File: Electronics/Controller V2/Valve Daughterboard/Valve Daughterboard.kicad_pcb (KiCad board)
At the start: 2 copper layers, 68.5 x 87.5 mm, 30 parts, among them J1 Conn_01x08, J10 Conn_01x10, J11 Conn_01x02, J12 Conn_01x02, J13 Conn_01x02, J14 Conn_01x02, J15 Conn_01x02, J16 Conn_01x02, J17 Conn_01x02, J18 Conn_01x02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

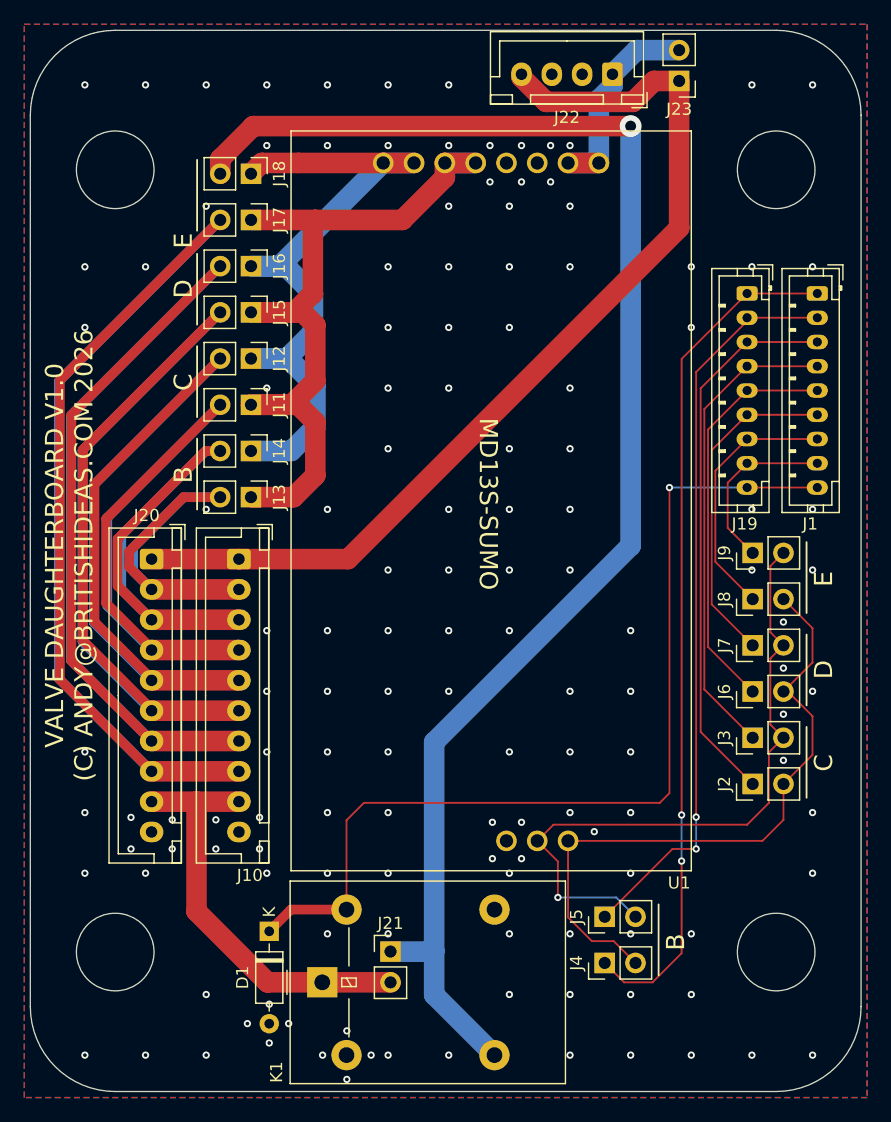
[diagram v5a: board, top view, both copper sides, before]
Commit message: Added jumper to bypass current sensing. Minor tweaks. Generated production files.
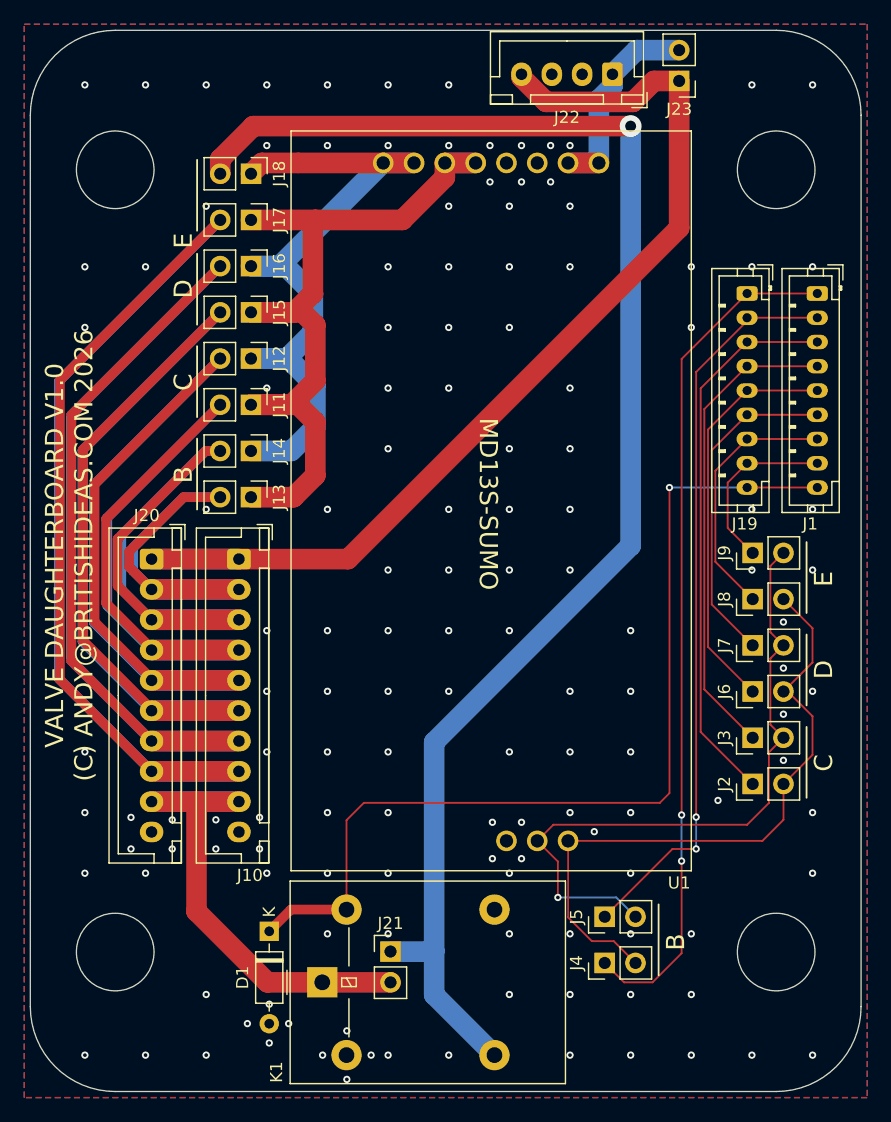
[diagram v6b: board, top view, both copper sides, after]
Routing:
- net /VALVE_C_MA: track 58.5 -> 65.7 mm
- net /VALVE_E_MB: track 34.7 -> 41.9 mm
- net /VALVE_D_MA: track 87.0 -> 94.2 mm
- net /VALVE_B_MB: track 45.5 -> 52.7 mm
- net /VALVE_B_MA: track 33.4 -> 40.6 mm
- net +12V: track 81.7 -> 88.9 mm
- net /VALVE_E_MA: track 115.4 -> 122.6 mm
- net /VALVE_D_MB: track 101.2 -> 108.4 mm
- net /VALVE_C_MB: track 72.8 -> 80.0 mm
- net GND: vias 138 -> 139
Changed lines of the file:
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@@
     (fp_line (start 24.95 3.4) (end 24.95 -2.35)
       (stroke (width 0.1) (type solid)) (layer "F.Fab"))
-    (pad "1" thru_hole roundrect (at 0 0 270) (size 1.7 1.95) (drill 0.95) (layers "*.Cu" "*.Mask") (roundrect_rratio 0.147059)
+    (pad "1" thru_hole roundrect (at 0 0 270) (size 1.7 1.95) (drill 0.95) (layers "*.Cu" "*.Mask") (roundrect_rratio 0.1470588235)
       (net 11 "+12V") (pinfunction "Pin_1") (pintype "passive"))
     (pad "2" thru_hole oval (at 2.5 0 270) (size 1.7 1.95) (drill 0.95) (layers "*.Cu" "*.Mask")
@@
     (fp_line (start 9.95 3.4) (end 9.95 -2.35)
       (stroke (width 0.1) (type solid)) (layer "F.Fab"))
-    (pad "1" thru_hole roundrect (at 0 0 180) (size 1.7 1.95) (drill 0.95) (layers "*.Cu" "*.Mask") (roundrect_rratio 0.147059)
+    (pad "1" thru_hole roundrect (at 0 0 180) (size 1.7 1.95) (drill 0.95) (layers "*.Cu" "*.Mask") (roundrect_rratio 0.1470588235)
       (net 26 "VDD") (pinfunction "Pin_1") (pintype "passive"))
     (pad "2" thru_hole oval (at 2.5 0 180) (size 1.7 1.95) (drill 0.95) (layers "*.Cu" "*.Mask")
@@
     (fp_line (start 17.95 2.8) (end 17.95 -1.7)
       (stroke (width 0.1) (type solid)) (layer "F.Fab"))
-    (pad "1" thru_hole roundrect (at 0 0 270) (size 1.2 1.75) (drill 0.75) (layers "*.Cu" "*.Mask") (roundrect_rratio 0.208333)
+    (pad "1" thru_hole roundrect (at 0 0 270) (size 1.2 1.75) (drill 0.75) (layers "*.Cu" "*.Mask") (roundrect_rratio 0.2083333333)
       (net 1 "/VALVE_B_DIR") (pinfunction "Pin_1") (pintype "passive"))
     (pad "2" thru_hole oval (at 2 0 270) (size 1.2 1.75) (drill 0.75) (layers "*.Cu" "*.Mask")
@@
     (fp_line (start 24.95 3.4) (end 24.95 -2.35)
       (stroke (width 0.1) (type solid)) (layer "F.Fab"))
-    (pad "1" thru_hole roundrect (at 0 0 270) (size 1.7 1.95) (drill 0.95) (layers "*.Cu" "*.Mask") (roundrect_rratio 0.147059)
+    (pad "1" thru_hole roundrect (at 0 0 270) (size 1.7 1.95) (drill 0.95) (layers "*.Cu" "*.Mask") (roundrect_rratio 0.1470588235)
       (net 11 "+12V") (pinfunction "Pin_1") (pintype "passive"))
     (pad "2" thru_hole oval (at 2.5 0 270) (size 1.7 1.95) (drill 0.95) (layers "*.Cu" "*.Mask")
@@
     (fp_line (start 17.95 2.8) (end 17.95 -1.7)
       (stroke (width 0.1) (type solid)) (layer "F.Fab"))
-    (pad "1" thru_hole roundrect (at 0 0 270) (size 1.2 1.75) (drill 0.75) (layers "*.Cu" "*.Mask") (roundrect_rratio 0.208333)
+    (pad "1" thru_hole roundrect (at 0 0 270) (size 1.2 1.75) (drill 0.75) (layers "*.Cu" "*.Mask") (roundrect_rratio 0.2083333333)
       (net 1 "/VALVE_B_DIR") (pinfunction "Pin_1") (pintype "passive"))
     (pad "2" thru_hole oval (at 2 0 270) (size 1.2 1.75) (drill 0.75) (layers "*.Cu" "*.Mask")
@@
   (segment (start 132.925 52.675) (end 131.2 54.4) (width 1.7) (layer "F.Cu") (net 11))
   (segment (start 135 64.8) (end 135 52.675) (width 1.7) (layer "F.Cu") (net 11))
+  (segment (start 98.7 92.1) (end 91.5 92.1) (width 1.7) (layer "B.Cu") (net 11))
   (segment (start 89.65 91.483874) (end 89.65 92.75) (width 0.8) (layer "F.Cu") (net 12))
   (segment (start 94.138874 86.995) (end 89.65 91.483874) (width 0.8) (layer "F.Cu") (net 12))
@@
   (segment (start 94.138874 86.995) (end 89.973 91.160874) (width 0.8) (layer "B.Cu") (net 12))
   (segment (start 89.973 93.073) (end 91.5 94.6) (width 0.8) (layer "B.Cu") (net 12))
+  (segment (start 98.7 94.6) (end 91.5 94.6) (width 1.7) (layer "B.Cu") (net 12))
   (segment (start 89.973 91.160874) (end 89.973 93.073) (width 0.8) (layer "B.Cu") (net 12))
   (segment (start 97.155 86.995) (end 94.138874 86.995) (width 0.8) (layer "B.Cu") (net 12))
@@
   (segment (start 95.952919 83.185) (end 89 90.137919) (width 0.8) (layer "B.Cu") (net 13))
   (segment (start 97.155 83.185) (end 95.952919 83.185) (width 0.8) (layer "B.Cu") (net 13))
+  (segment (start 98.7 97.1) (end 91.5 97.1) (width 1.7) (layer "B.Cu") (net 13))
   (segment (start 89 90.137919) (end 89 94.6) (width 0.8) (layer "B.Cu") (net 13))
   (segment (start 97.155 79.375) (end 87.746004 88.783996) (width 0.8) (layer "F.Cu") (net 14))
@@
   (segment (start 97.155 79.375) (end 87.85 88.68) (width 0.8) (layer "B.Cu") (net 14))
   (segment (start 87.85 88.68) (end 87.85 95.95) (width 0.8) (layer "B.Cu") (net 14))
+  (segment (start 98.7 99.6) (end 91.5 99.6) (width 1.7) (layer "B.Cu") (net 14))
   (segment (start 87.85 95.95) (end 91.5 99.6) (width 0.8) (layer "B.Cu") (net 14))
   (segment (start 91.5 102.1) (end 98.7 102.1) (width 1.7) (layer "F.Cu") (net 15))
@@
   (segment (start 86.794008 85.925992) (end 86.794008 97.269008) (width 0.8) (layer "F.Cu") (net 15))
   (segment (start 91.5 101.975) (end 91.5 102.1) (width 0.8) (layer "F.Cu") (net 15))
+  (segment (start 98.7 102.1) (end 91.5 102.1) (width 1.7) (layer "B.Cu") (net 15))
   (segment (start 97.155 75.565) (end 86.754 85.966) (width 0.8) (layer "B.Cu") (net 15))
   (segment (start 86.754 97.354) (end 91.5 102.1) (width 0.8) (layer "B.Cu") (net 15))
@@
   (segment (start 97.16 71.755) (end 85.842012 83.072988) (width 0.8) (layer "F.Cu") (net 16))
   (segment (start 85.802 98.902) (end 91.5 104.6) (width 0.8) (layer "B.Cu") (net 16))
+  (segment (start 98.7 104.6) (end 91.5 104.6) (width 1.7) (layer "B.Cu") (net 16))
   (segment (start 97.16 71.755) (end 85.802 83.113) (width 0.8) (layer "B.Cu") (net 16))
   (segment (start 85.802 83.113) (end 85.802 98.902) (width 0.8) (layer "B.Cu") (net 16))
@@
   (segment (start 84.85 100.45) (end 91.5 107.1) (width 0.8) (layer "B.Cu") (net 17))
   (segment (start 84.85 80.255) (end 84.85 100.45) (width 0.8) (layer "B.Cu") (net 17))
+  (segment (start 98.7 107.1) (end 91.5 107.1) (width 1.7) (layer "B.Cu") (net 17))
   (segment (start 97.16 67.945) (end 84.85 80.255) (width 0.8) (layer "B.Cu") (net 17))
   (segment (start 97.16 64.135) (end 83.937983 77.357017) (width 0.8) (layer "F.Cu") (net 18))
@@
   (segment (start 83.85 101.95) (end 91.5 109.6) (width 0.8) (layer "B.Cu") (net 18))
   (segment (start 83.85 77.445) (end 83.85 101.95) (width 0.8) (layer "B.Cu") (net 18))
+  (segment (start 98.7 109.6) (end 91.5 109.6) (width 1.7) (layer "B.Cu") (net 18))
   (segment (start 95.2 112.1) (end 98.7 112.1) (width 1.7) (layer "F.Cu") (net 19))
   (segment (start 91.5 112.1) (end 95.2 112.1) (width 1.7) (layer "F.Cu") (net 19))
@@
   (segment (start 95.2 112.1) (end 95.2 121.145261) (width 1.7) (layer "F.Cu") (net 19))
   (segment (start 105.5725 127) (end 111.2 127) (width 1.7) (layer "F.Cu") (net 19))
+  (segment (start 98.7 112.1) (end 91.5 112.1) (width 1.7) (layer "B.Cu") (net 19))
   (via (at 101.2 132) (size 0.6) (drill 0.3) (layers "F.Cu" "B.Cu") (free) (net 20))
   (via (at 143.595 101.09) (size 0.6) (drill 0.3) (layers "F.Cu" "B.Cu") (free) (net 20))
@@
   (via (at 111 103) (size 0.6) (drill 0.3) (layers "F.Cu" "B.Cu") (free) (net 20))
   (via (at 119.4 58) (size 0.6) (drill 0.3) (layers "F.Cu" "B.Cu") (free) (net 20))
+  (via (at 138.2 112) (size 0.6) (drill 0.3) (layers "F.Cu" "B.Cu") (free) (net 20))
   (via (at 119.6 113.8) (size 0.6) (drill 0.3) (layers "F.Cu" "B.Cu") (free) (net 20))
   (via (at 131 113) (size 0.6) (drill 0.3) (layers "F.Cu" "B.Cu") (free) (net 20))
